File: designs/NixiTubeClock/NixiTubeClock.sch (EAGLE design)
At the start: 17 parts, among them IC1 74141N, IC2 74HCT595D, IC3 74141N, IC4 74141N, IC5 74HCT595D, IC6 74141N

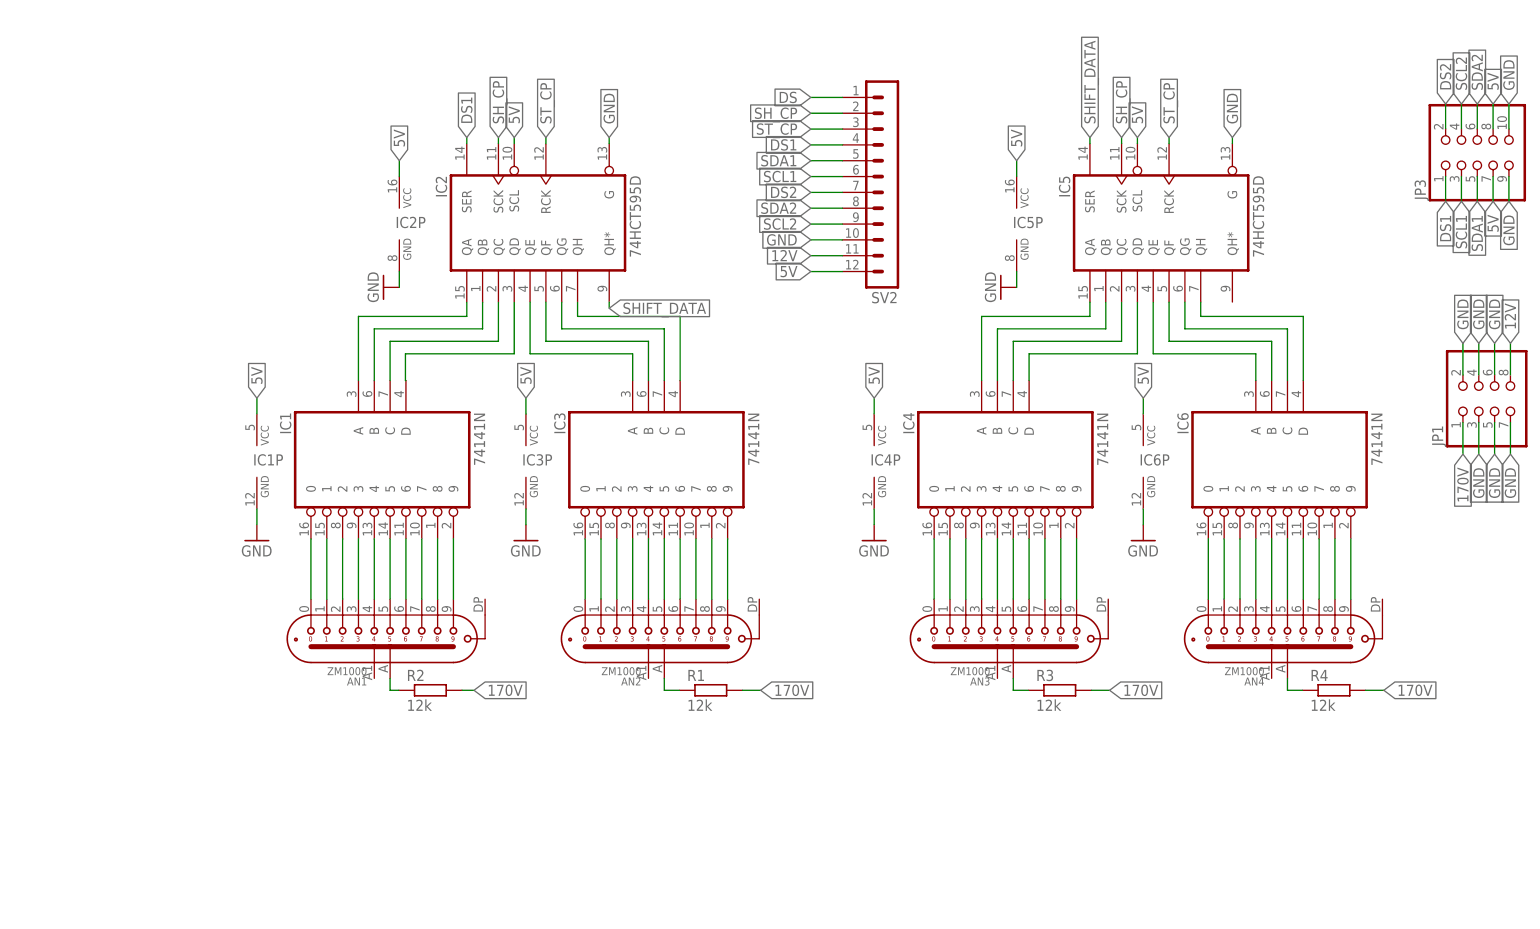
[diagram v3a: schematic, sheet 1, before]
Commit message: added nixiClock brd and sheet with new design OSH
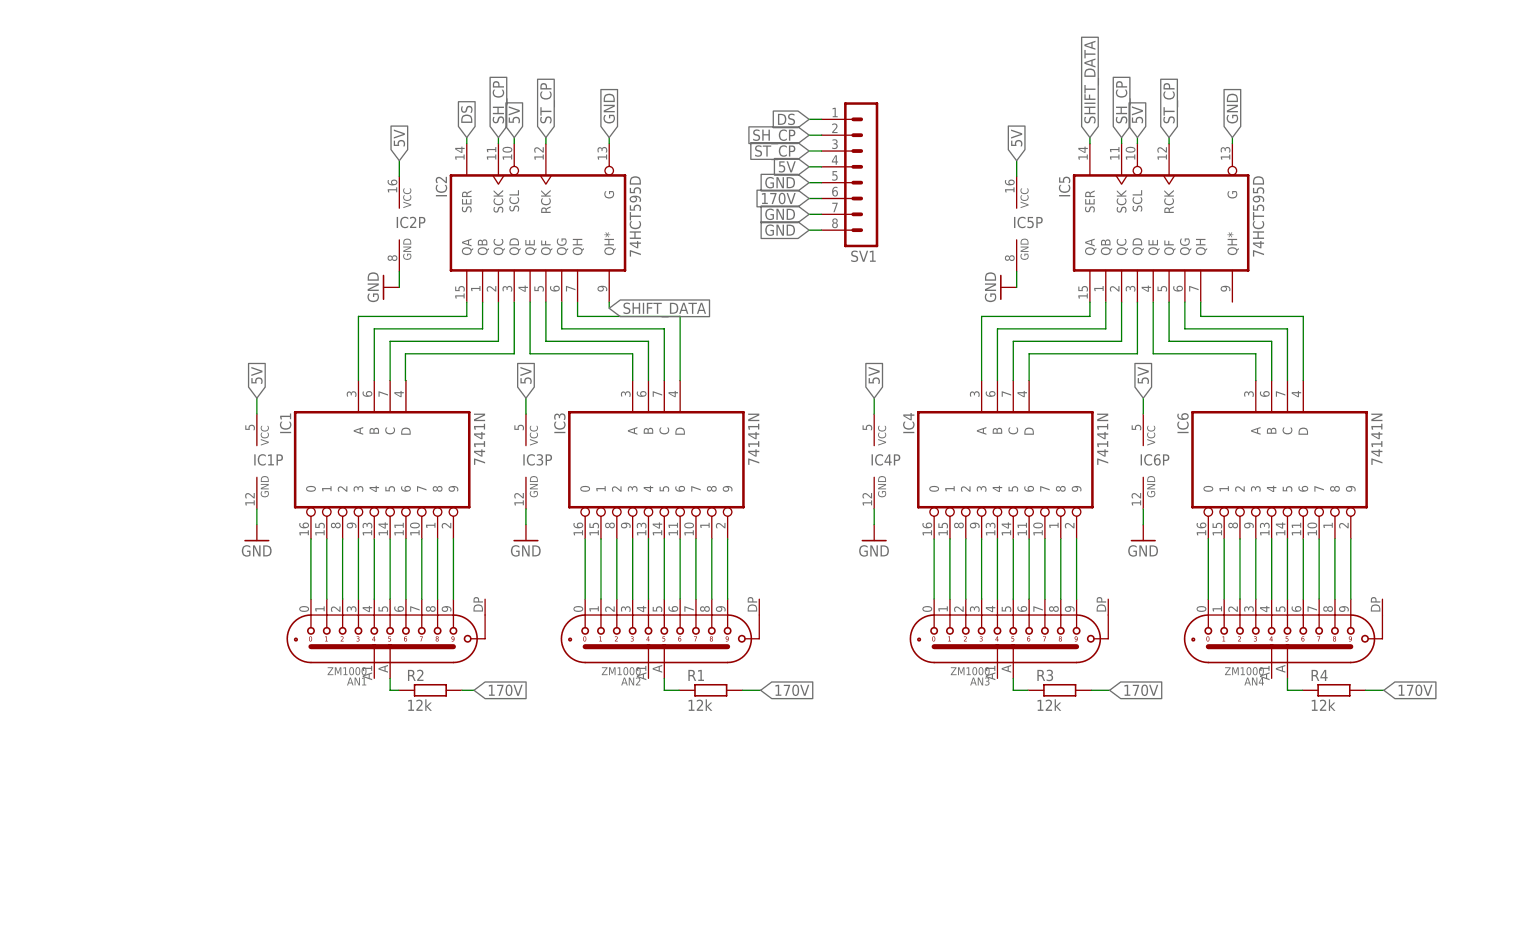
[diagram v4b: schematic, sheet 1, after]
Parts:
- removed JP1: (no value), pinhead:PINHD-2X4/90
- removed JP3: (no value), pinhead:PINHD-2X5/90
- removed SV2: (no value), con-lstb:MA12-1
- added SV1: (no value), con-lstb:MA08-1
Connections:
- removed net 12V: JP1.8, SV2.11
- removed net DS1: IC2A.SER, JP3.1, SV2.4
- removed net DS2: JP3.2, SV2.7
- removed net SCL1: JP3.3, SV2.6
- removed net SCL2: JP3.4, SV2.9
- removed net SDA1: JP3.5, SV2.5
- removed net SDA2: JP3.6, SV2.8
- net 170V: now also SV1.6; no longer JP1.1
- net 5V: now also SV1.4; no longer JP3.7, JP3.8, SV2.12
- net DS: now also IC2A.SER, SV1.1; no longer SV2.1
- net GND: now also SV1.5, SV1.7, SV1.8; no longer JP1.2, JP1.3, JP1.4, JP1.5, JP1.6, JP1.7, JP3.10, JP3.9, SV2.10
- net SH_CP: now also SV1.2; no longer SV2.2
- net ST_CP: now also SV1.3; no longer SV2.3
